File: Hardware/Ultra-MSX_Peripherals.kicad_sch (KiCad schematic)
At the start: 56 parts, among them J4 OST_Conn_302-S341, J5 Amphenol_L17H1220134, J6 DIN-8_SDF-80J, J7 AdamTech_USB3-2_USB_C_Recepta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, J8 SDF-130J, J9 Ultra-video-daughter, Q2 MMBT2907AM3T5G, U49 LM311

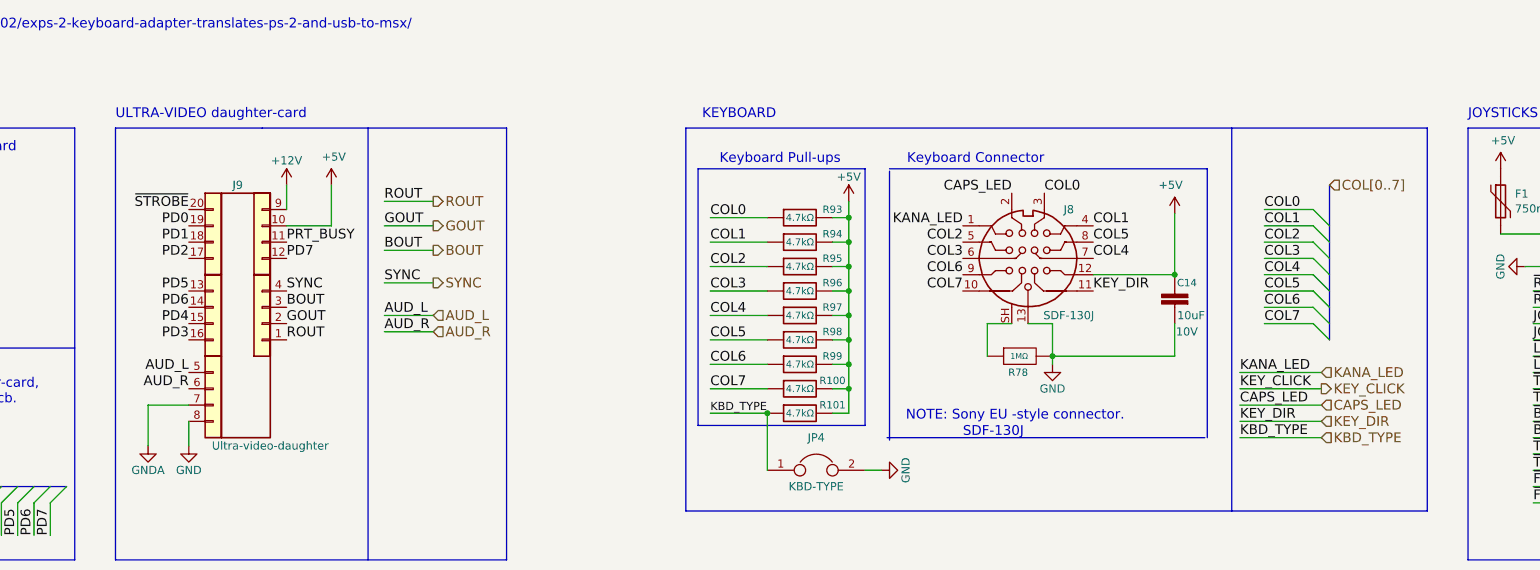
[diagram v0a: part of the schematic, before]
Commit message: Routed the VDP-board further, as well as making it a 4-layer board - also added an exception in the gitignore, for big images.
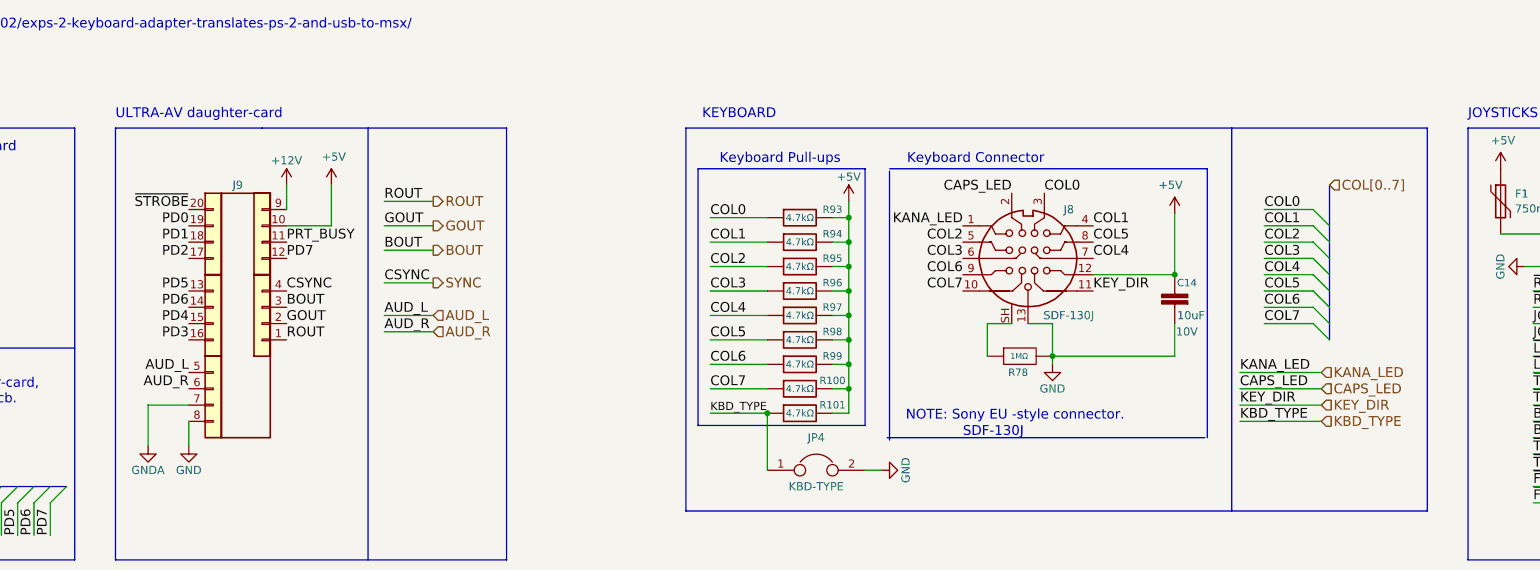
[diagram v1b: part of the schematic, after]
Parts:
- J9: value Ultra-video-daughter -> (none); symbol Ultra-MSX:Ultra-video-daughter -> Ultra-MSX:Ultra-av-daughter
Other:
- note added: "ULTRA-AV daughter-card"
- note removed: "ULTRA-VIDEO daughter-card"
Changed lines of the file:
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@@
     (stroke (width 0) (type default) (color 0 0 0 0))
   )
-  (wire (pts (xy 243.84 62.23) (xy 256.54 62.23))
+  (wire (pts (xy 243.84 59.69) (xy 256.54 59.69))
     (stroke (width 0) (type default) (color 0 0 0 0))
   )
@@
     (stroke (width 0) (type default) (color 0 0 0 0))
   )
-  (wire (pts (xy 243.84 67.31) (xy 256.54 67.31))
+  (wire (pts (xy 243.84 64.77) (xy 256.54 64.77))
     (stroke (width 0) (type default) (color 0 0 0 0))
   )
@@
     (stroke (width 0) (type default) (color 0 0 0 0))
   )
-  (wire (pts (xy 243.84 64.77) (xy 256.54 64.77))
+  (wire (pts (xy 243.84 62.23) (xy 256.54 62.23))
     (stroke (width 0) (type default) (color 0 0 0 0))
   )
@@
     (stroke (width 0) (type default) (color 0 0 0 0))
   )
-  (wire (pts (xy 243.84 59.69) (xy 256.54 59.69))
-    (stroke (width 0) (type default) (color 0 0 0 0))
-  )
   (wire (pts (xy 240.03 118.11) (xy 240.03 115.57))
     (stroke (width 0) (type default) (color 0 0 0 0))
@@
     (effects (font (size 1.524 1.524)) (justify left bottom))
   )
-  (text "ULTRA-VIDEO daughter-card" (at 68.58 17.78 0)
+  (text "ULTRA-AV daughter-card" (at 68.58 17.78 0)
     (effects (font (size 1.524 1.524)) (justify left bottom))
   )
@@
     (effects (font (size 1.524 1.524)) (justify left bottom))
   )
-  (label "SYNC" (at 95.25 44.45 0)
+  (label "CSYNC" (at 95.25 44.45 0)
     (effects (font (size 1.524 1.524)) (justify left bottom))
   )
@@
     (effects (font (size 1.524 1.524)) (justify left bottom))
   )
-  (label "KEY_DIR" (at 243.84 64.77 0)
+  (label "KEY_DIR" (at 243.84 62.23 0)
     (effects (font (size 1.524 1.524)) (justify left bottom))
   )
@@
     (effects (font (size 1.524 1.524)) (justify left bottom))
   )
-  (label "CAPS_LED" (at 243.84 62.23 0)
+  (label "CAPS_LED" (at 243.84 59.69 0)
     (effects (font (size 1.524 1.524)) (justify left bottom))
   )
@@
     (effects (font (size 1.524 1.524)) (justify left bottom))
   )
-  (label "SYNC" (at 110.49 43.18 0)
+  (label "CSYNC" (at 110.49 43.18 0)
     (effects (font (size 1.524 1.524)) (justify left bottom))
   )
@@
     (effects (font (size 1.524 1.524)) (justify left bottom))
   )
-  (label "KEY_CLICK" (at 243.84 59.69 0)
-    (effects (font (size 1.524 1.524)) (justify left bottom))
-  )
   (label "~{DRVSB}" (at 247.65 120.65 0)
     (effects (font (size 1.524 1.524)) (justify left bottom))
@@
     (effects (font (size 1.524 1.524)) (justify left bottom))
   )
-  (label "KBD_TYPE" (at 243.84 67.31 0)
+  (label "KBD_TYPE" (at 243.84 64.77 0)
     (effects (font (size 1.524 1.524)) (justify left bottom))
   )
@@
     (effects (font (size 1.524 1.524)) (justify left))
   )
-  (hierarchical_label "KEY_DIR" (shape input) (at 256.54 64.77 0)
+  (hierarchical_label "KEY_DIR" (shape input) (at 256.54 62.23 0)
     (effects (font (size 1.524 1.524)) (justify left))
   )
@@
     (effects (font (size 1.524 1.524)) (justify left))
   )
-  (hierarchical_label "KBD_TYPE" (shape input) (at 256.54 67.31 0)
+  (hierarchical_label "KBD_TYPE" (shape input) (at 256.54 64.77 0)
     (effects (font (size 1.524 1.524)) (justify left))
   )
@@
     (effects (font (size 1.524 1.524)) (justify left))
   )
-  (hierarchical_label "CAPS_LED" (shape input) (at 256.54 62.23 0)
+  (hierarchical_label "CAPS_LED" (shape input) (at 256.54 59.69 0)
     (effects (font (size 1.524 1.524)) (justify left))
   )
@@
     (effects (font (size 1.524 1.524)) (justify left))
   )
-  (hierarchical_label "KEY_CLICK" (shape output) (at 256.54 59.69 0)
-    (effects (font (size 1.524 1.524)) (justify left))
-  )
   (hierarchical_label "KANA_LED" (shape input) (at 256.54 57.15 0)
     (effects (font (size 1.524 1.524)) (justify left))
@@
     (pin "2")
   )
-  (symbol (lib_id "Ultra-MSX:Ultra-video-daughter") (at 87.63 46.99 0) (unit 1)
+  (symbol (lib_id "Ultra-MSX:Ultra-av-daughter") (at 87.63 46.99 0) (unit 1)
     (in_bom no) (on_board yes)
     (property "Reference" "J9" (id 0) (at 87.63 27.94 0))
-    (property "Value" "Ultra-video-daughter" (id 1) (at 92.71 68.58 0))
+    (property "Value" "" (id 1) (at 92.71 68.58 0))
     (property "Footprint" "Ultra-MSX:Ultra-video-daughter" (id 2) (at 87.63 72.39 0)
       (effects (font (size 1.27 1.27)) hide)

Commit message: Finished the VDP-board, finished up the mixer-section, removed the buffer-pins from the FPGA, and instead added external buffers for the slots, designed a marquee-block with the Ultra-MSX logo, designed the logotype, andmultiple other changes.
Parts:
- J9: value (none) -> Ultra-av-daughter
- RY2: value IM43GR -> TE_IM43GR; footprint SamacSys_Parts:SMTGULLWINGS -> LRJ:Relay_DPDT_AXICOM_IMSeries_GullWing; symbol LRJ-parts:IM43GR -> LRJ-parts:TE_IM43GR; Current Rating (none) -> 2A; MPN (none) -> IM43GR; Manufacturer (none) -> TE Connectivity; Voltage Rating (none) -> 250V
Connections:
- net GND: now also J5.SH; no longer J5.0 (SH)
- net SYNC renamed CSYNC
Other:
- note added: "See 'Ultra-AV' daughter-card for schematics on connector."
- note removed: "See 'Ultra-video' daughter-card for schematics on connector."
- moved on the sheet: C14, C29, F1, J5, J7, J8, JP4, R100, R101, R102, R103, R104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

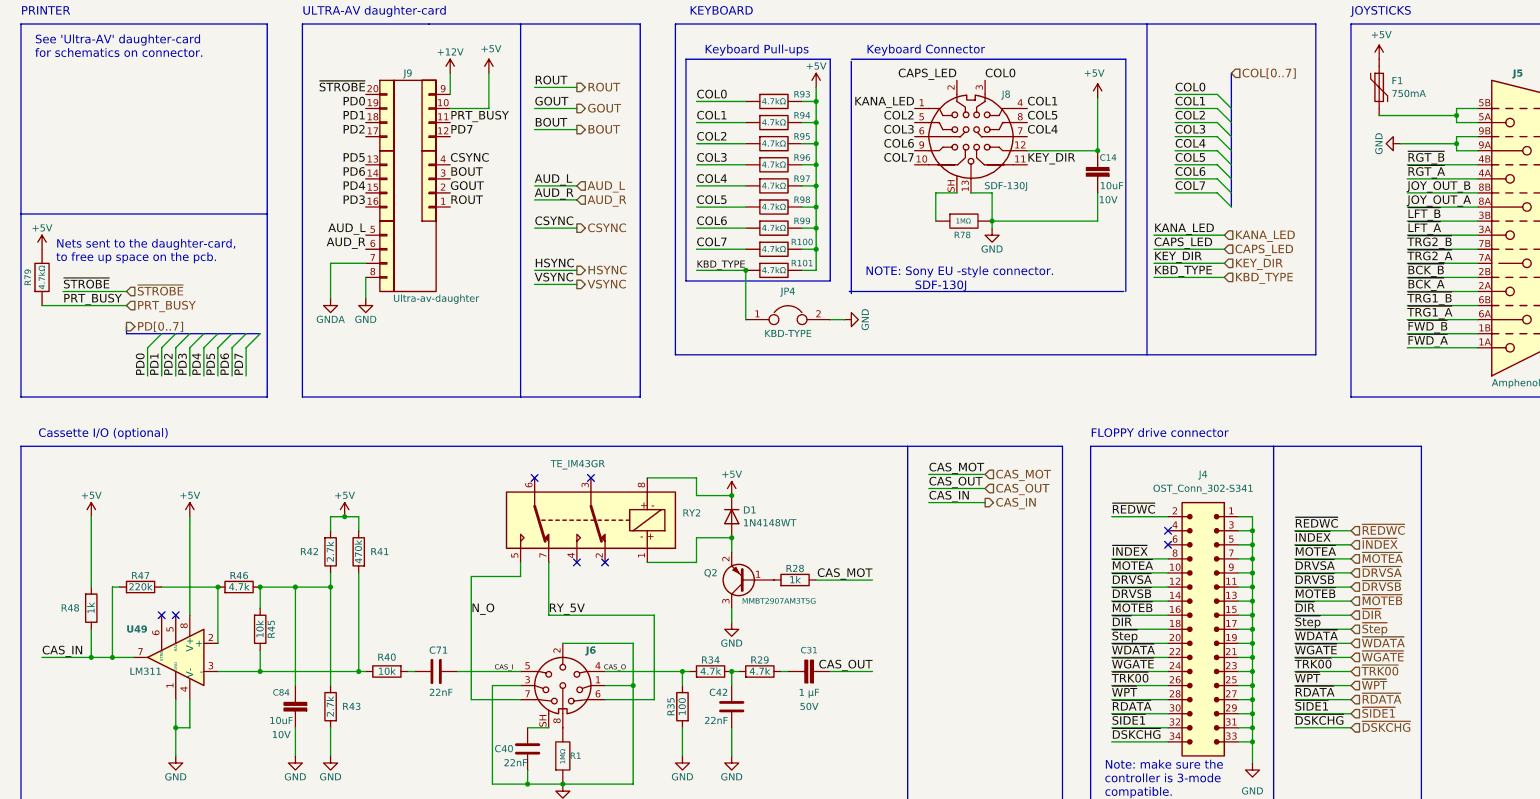
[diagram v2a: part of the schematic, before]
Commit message: Started routing the Cassette-player on the PCB.
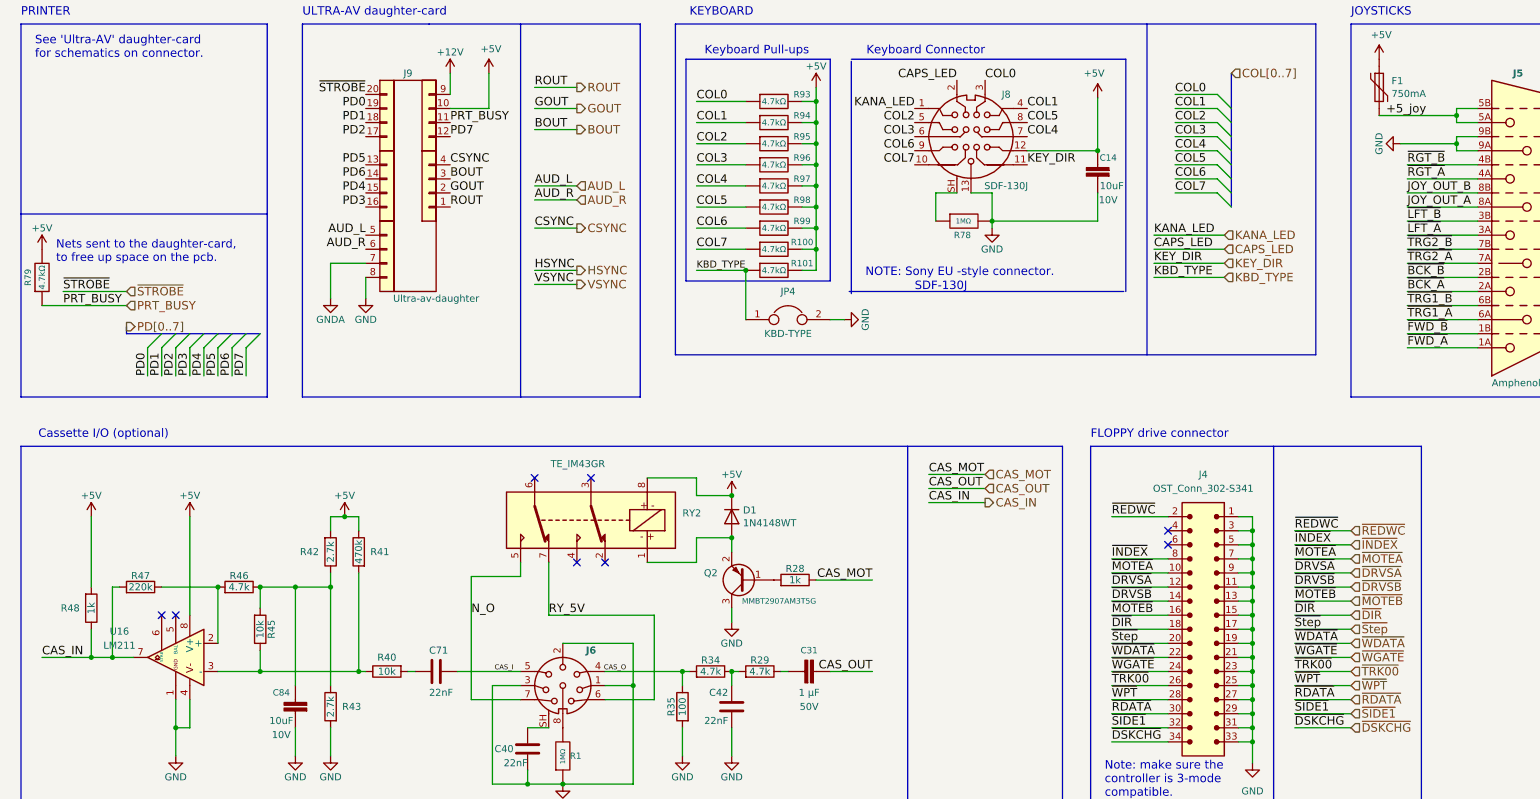
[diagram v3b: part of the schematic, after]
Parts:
- removed U49: LM311, Ultra-MSX:IC_DIP8_300, symbol Ultra-MSX:LM311
- added U16: LM211, Package_SO:SOIC-8_3.9x4.9mm_P1.27mm, symbol LRJ-parts:LM211
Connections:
- net +5V: now also U16.8 (V+)
- net CAS_IN: now also U16.7 (COL_OUT)
- net GND: now also U16.1 (GND), U16.4 (V-)
- net at R46.2, R47.1: now also U16.2 (+)
- net at R40.1, R41.2, R45.1: now also U16.3 (-)
- net +5_joy: now reaches F1.2, J5.5A (5), J5.5B (5)
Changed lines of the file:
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@@
+    (effects (font (size 1.524 1.524)) (justify left bottom))
+  )
+  (label "+5_joy" (at 264.16 35.56 0)
     (effects (font (size 1.524 1.524)) (justify left bottom))
   )
@@
     )
     (pin "1")
-  )
-  (symbol (lib_id "Ultra-MSX:LM311") (at 45.72 133.35 0) (mirror y) (unit 1)
-    (in_bom yes) (on_board yes)
-    (property "Reference" "U49" (id 0) (at 40.64 128.27 0)
-      (effects (font (size 1.27 1.27) bold) (justify left))
-    )
-    (property "Value" "LM311" (id 1) (at 43.18 135.89 0)
-      (effects (font (size 1.27 1.27)) (justify left))
-    )
-    (property "Footprint" "Ultra-MSX:IC_DIP8_300" (id 2) (at 45.72 133.35 0)
-      (effects (font (size 1.27 1.27)) hide)
-    )
-    (property "Datasheet" "" (id 3) (at 45.72 133.35 0)
-      (effects (font (size 1.27 1.27)) hide)
-    )
-    (pin "1")
-    (pin "2")
-    (pin "3")
-    (pin "4")
-    (pin "5")
-    (pin "6")
-    (pin "7")
-    (pin "8")
   )
   (symbol (lib_id "Device:R") (at 30.48 124.46 0) (mirror x) (unit 1)
@@
     (pin "1")
   )
+  (symbol (lib_id "LRJ-parts:LM211") (at 45.72 133.35 0) (mirror y) (unit 1)
+    (in_bom yes) (on_board yes) (fields_autoplaced)
+    (property "Reference" "U16" (id 0) (at 35.56 128.651 0))
+    (property "Value" "LM211" (id 1) (at 35.56 131.191 0))
+    (property "Footprint" "Package_SO:SOIC-8_3.9x4.9mm_P1.27mm" (id 2) (at 15.24 138.43 0)
+      (effects (font (size 1.27 1.27)) hide)
+    )
+    (property "Datasheet" "https://www.ti.com/general/docs/suppproductinfo.tsp?distId=10&gotoUrl=https%3A%2F%2Fwww.ti.com%2Flit%2Fgpn%2Flm211" (id 3) (at -25.4 140.97 0)
+      (effects (font (size 1.27 1.27)) hide)
+    )
+    (property "Description" "IC DIFF COMPARATOR W/STRB 8-SOIC" (id 4) (at 17.78 135.89 0)
+      (effects (font (size 1.27 1.27)) hide)
+    )
+    (property "Manufacturer" "Texas Instruments" (id 5) (at 25.4 125.73 0)
+      (effects (font (size 1.27 1.27)) hide)
+    )
+    (property "MPN" "LM211DR" (id 6) (at 30.48 128.27 0)
+      (effects (font (size 1.27 1.27)) hide)
+    )
+    (property "Voltage Rating" "30V" (id 7) (at 33.02 130.81 0)
+      (effects (font (size 1.27 1.27)) hide)
+    )
+    (property "Current Rating" "50 mA" (id 8) (at 30.48 133.35 0)
+      (effects (font (size 1.27 1.27)) hide)
+    )
+    (pin "1")
+    (pin "2")
+    (pin "3")
+    (pin "4")
+    (pin "5")
+    (pin "6")
+    (pin "7")
+    (pin "8")
+  )
   (symbol (lib_id "LRJ-parts:R_RC0603FR-074K7L") (at 330.2 67.31 0) (unit 1)
